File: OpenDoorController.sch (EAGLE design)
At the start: 1 part, among them U1 ATMEGA2560AU

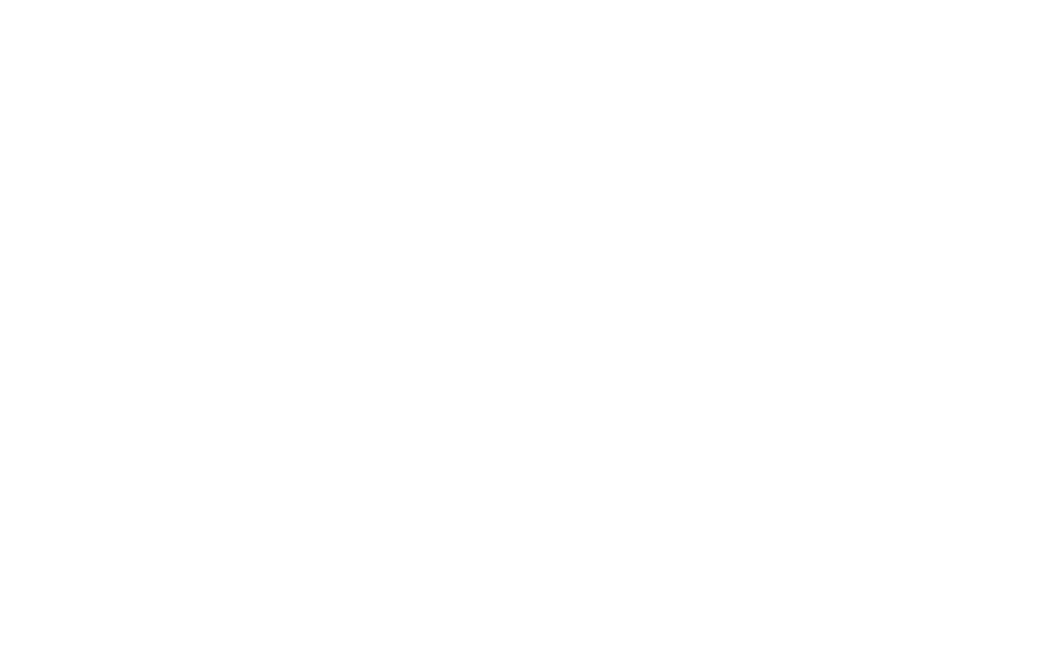
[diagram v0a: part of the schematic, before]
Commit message: Started implementing SMPS and created custom library for esoteric parts
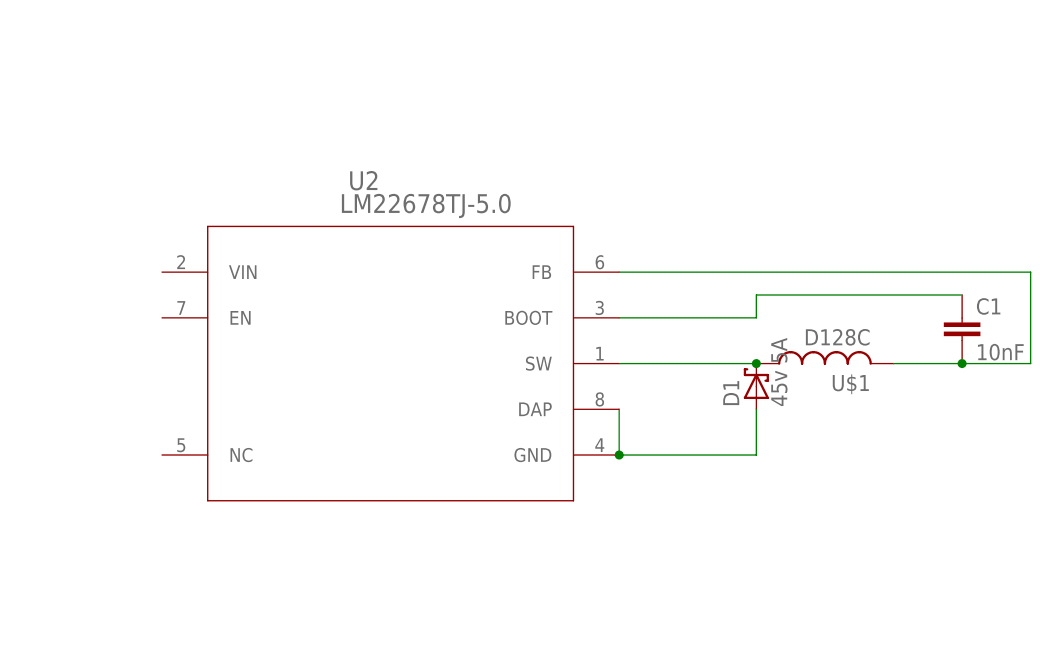
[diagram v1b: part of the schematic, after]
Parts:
- added C1: 10nF, rcl:C-EUC1206
- added D1: 45v 5A, diode:SCHOTTKY-DIODESMC
- added U$1: D128C, CustomSymbols:D128C
- added U2: LM22678TJ-5.0, CustomSymbols:LM22678TJ-5.0
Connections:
- new net N$1: D1.C, U$1.1, U2.SW
- new net N$2: C1.1, U2.BOOT
- new net N$3: C1.2, U$1.2, U2.FB
- new net N$4: D1.A, U2.DAP, U2.GND
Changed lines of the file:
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@@
 <?xml version="1.0" encoding="utf-8"?>
 <!DOCTYPE eagle SYSTEM "eagle.dtd">
-<eagle version="6.1">
+<eagle version="6.2">
 <drawing>
 <settings>
@@
 <parts>
 <part name="U1" library="SparkFun" deviceset="ATMEGA2560" device="AU"/>
+<part name="U2" library="CustomSymbols" deviceset="LM22678TJ-5.0" device=""/>
+<part name="U$1" library="CustomSymbols" deviceset="D128C" device="">
+<attribute name="STOCKNUM" value="724-4890"/>
+<attribute name="SUPPLIER" value="RS Components"/>
+</part>
+<part name="C1" library="rcl" deviceset="C-EU" device="C1206" value="10nF"/>
+<part name="D1" library="diode" deviceset="SCHOTTKY-DIODE" device="SMC" value="45v 5A"/>
 </parts>
 <sheets>
@@
 <instances>
 <instance part="U1" gate="1" x="60.96" y="96.52"/>
+<instance part="U2" gate="A" x="144.78" y="68.58"/>
+<instance part="U$1" gate="G$1" x="218.44" y="58.42" rot="R90">
+<attribute name="STOCKNUM" x="218.44" y="58.42" size="1.778" layer="96" rot="R90" display="off"/>
+<attribute name="SUPPLIER" x="218.44" y="58.42" size="1.778" layer="96" rot="R90" display="off"/>
+</instance>
+<instance part="C1" gate="G$1" x="233.68" y="63.5"/>
+<instance part="D1" gate="G$1" x="210.82" y="55.88" rot="R90"/>
 </instances>
 <busses>
 </busses>
 <nets>
+<net name="N$1" class="0">
+<segment>
+<pinref part="U2" gate="A" pin="SW"/>
+<pinref part="U$1" gate="G$1" pin="1"/>
+<wire x1="195.58" y1="58.42" x2="210.82" y2="58.42" width="0.1524" layer="91"/>
+<pinref part="D1" gate="G$1" pin="C"/>
+<junction x="210.82" y="58.42"/>
+</segment>
+</net>
+<net name="N$2" class="0">
+<segment>
+<pinref part="U2" gate="A" pin="BOOT"/>
+<wire x1="195.58" y1="63.5" x2="210.82" y2="63.5" width="0.1524" layer="91"/>
+<wire x1="210.82" y1="63.5" x2="210.82" y2="66.04" width="0.1524" layer="91"/>
+<pinref part="C1" gate="G$1" pin="1"/>
+<wire x1="210.82" y1="66.04" x2="233.68" y2="66.04" width="0.1524" layer="91"/>
+</segment>
+</net>
+<net name="N$3" class="0">
+<segment>
+<pinref part="U$1" gate="G$1" pin="2"/>
+<pinref part="C1" gate="G$1" pin="2"/>
+<wire x1="226.06" y1="58.42" x2="233.68" y2="58.42" width="0.1524" layer="91"/>
+<pinref part="U2" gate="A" pin="FB"/>
+<wire x1="195.58" y1="68.58" x2="241.3" y2="68.58" width="0.1524" layer="91"/>
+<wire x1="241.3" y1="68.58" x2="241.3" y2="58.42" width="0.1524" layer="91"/>
+<wire x1="241.3" y1="58.42" x2="233.68" y2="58.42" width="0.1524" layer="91"/>
+<junction x="233.68" y="58.42"/>
+</segment>
+</net>
+<net name="N$4" class="0">
+<segment>
+<pinref part="U2" gate="A" pin="GND"/>
+<pinref part="D1" gate="G$1" pin="A"/>
+<wire x1="195.58" y1="48.26" x2="210.82" y2="48.26" width="0.1524" layer="91"/>
+<wire x1="210.82" y1="48.26" x2="210.82" y2="53.34" width="0.1524" layer="91"/>
+<pinref part="U2" gate="A" pin="DAP"/>
+<wire x1="195.58" y1="53.34" x2="195.58" y2="48.26" width="0.1524" layer="91"/>
+<junction x="195.58" y="48.26"/>
+</segment>
+</net>
 </nets>
 </sheet>
 </sheets>
+<errors>
+</errors>
 </schematic>
 </drawing>

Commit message: Cleanup, AVR support stuff and WIZnet stuff started
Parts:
- added C2: 180uF, rcl:CPOL-EU153CLV-0810
- added C3, C4, C5, C6: 100nF, rcl:C-EUC0805
- added COL, FDX, LINK, RX, SPD, TX: (no value), led:LEDCHIPLED_0805
- added IC1: DS3231/SO, adafruit:DS3231/SO
- added R1: 1M, rcl:R-US_M1206
- added RESET: (no value), SparkFun:TAC_SWITCHSMD
- added U$2: (no value), adafruit:CR2032SMT
- added U$3: AVR_SPI_PROG2SMD, SparkFun:AVR_SPI_PROG2SMD
- added U3: (no value), SparkFun:W5100
- added Y1: RESONATORSMD, SparkFun:RESONATORSMD
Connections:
- new net (AREF): C6.1, U1.AREF
- new net (AVR_RESET): RESET.3, RESET.4, U$3.5, U1.RESET
- new net (MISO): U$3.9, U1.(MISO/PCINT3)PB3, U3.MISO
- new net (MOSI): U$3.1, U1.(MOSI/PCINT2)PB2, U3.MOSI
- new net (SCL): IC1.SCL, U1.(SCL/INT0)PD0
- new net (SCLK): U$3.7, U1.(SCK/PCINT1)PB1, U3.SCLK
- new net (SDA): IC1.SDA, U1.(SDA/INT1)PD1
- new net +3V3: U3.3V3A, U3.3V3D@0, U3.3V3D@1, U3.3V3D@2
- new net +5V: C1.2, C2.+, C3.1, C4.1, C5.1, U$1.2, U$3.2, U1.AVCC, U1.VCC, U1.VCC3, U2.FB
- new net GND: C2.-, C3.2, C4.2, C5.2, C6.2, COL.C, D1.A, FDX.C, IC1.GND, IC1.NC, IC1.NC1, IC1.NC2, IC1.NC3, IC1.NC4, IC1.NC5, IC1.NC6, IC1.NC7, LINK.C, RESET.1, RX.C, SPD.C, TX.C, U$2.+, U$2.+1, U$3.10, U$3.4, U$3.6, U$3.8, U1.AGND, U1.GND, U1.GND3, U2.DAP, U2.GND, U3.ADDR0, U3.ADDR1, U3.ADDR10, U3.ADDR11, U3.ADDR12, U3.ADDR13, U3.ADDR14, U3.ADDR2, U3.ADDR3, U3.ADDR4, U3.ADDR5, U3.ADDR6, U3.ADDR7, U3.ADDR8, U3.ADDR9, U3.DATA0, U3.DATA1, U3.DATA2, U3.DATA3, U3.DATA4, U3.DATA5, U3.DATA6, U3.DATA7, U3.GNDA@0, U3.GNDA@1, U3.GNDA@2, U3.GNDD@0, U3.GNDD@1, U3.GNDD@2, U3.GNDD@3, U3.GNDD@4, U3.GNDD@5, U3.OPMODE0, U3.OPMODE1, U3.OPMODE2, U3.TEST0, U3.TEST1, U3.TEST2, U3.TEST3, Y1.2
- new net N$10: IC1.VBAT, U$2.-
- new net N$16: LINK.A, U3.LINKLED
- new net N$18: SPD.A, U3.SPDLED
- new net N$19: FDX.A, U3.FDXLED
- new net N$20: COL.A, U3.COLLED
- new net N$21: RX.A, U3.RXLED
- new net N$22: TX.A, U3.TXLED
- new net N$5: U3.1V8A@0, U3.1V8A@1, U3.1V8D@0, U3.1V8D@1, U3.1V8D@2, U3.1V8D@3, U3.1V8OUT
- new net VCC: U2.VIN
- net N$3: now also R1.1, U1.XTAL1, Y1.3; no longer C1.2, U$1.2, U2.FB
- net N$4: now also R1.2, U1.XTAL2, Y1.1; no longer D1.A, U2.DAP, U2.GND
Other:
- moved on the sheet: C1, D1, U$1, U2

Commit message: More stuff implemented, I should sleep.
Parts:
- removed FDX, LINK: (no value), led:LEDCHIPLED_0805
- added C10, C11, C12: 0.1uF, rcl:C-EUC0805
- added C13: 470pF, rcl:C-EUC0805
- added C14: 2.2uF, rcl:C-EUC0805
- added C7, C8: 22pF, rcl:C-EUC0805
- added C9: 100nF, rcl:C-EUC0805
- added JP1: FTDI_BASICPTH, SparkFun:FTDI_BASICPTH
- added Q1: 25MHz, crystal:CRYSTALSM49
- added Q2: IRLML5203, transistor-power:IRLML5203
- added R10, R11, R12, R7, R8, R9: 470R, rcl:R-US_M0805
- added R13: 100R, rcl:R-US_M0805
- added R14: 10K, pot:TRIM_US-SM-42/43W
- added R15: 12K, rcl:R-US_M0805
- added R16: 300R, rcl:R-US_M0805
- added R17: 1k, rcl:R-US_M0805
- added R2: 1M, rcl:R-US_M1206
- added R3, R4, R5, R6: 49.9, rcl:R-US_M0805
- added STRIKE: (no value), con-wago-500:W237-102
- added U4: MAGJACK-POE, SparkFun:MAGJACK-POE
- added U5: MIC5205-3.3BM, SparkFun:V_REG_LDOSMD
- added X1: HD44780LCD-1602, adafruit:HD44780LCD-1602
- U$3: value AVR_SPI_PROG2SMD -> AVR_SPI_PROG2PTH2; device SparkFun:AVR_SPI_PROG2SMD -> SparkFun:AVR_SPI_PROG2PTH2
- Y1: value RESONATORSMD -> CSTCE16
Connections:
- net (AREF) renamed N$6
- new net (RX0): JP1.2, U1.(RXD0/PCIN8)PE0
- new net (RX1): U1.(SS/PCINT0)PB0
- new net (TX0): JP1.3, U1.(TXD0)PE1
- new net (TX1): U1.PH6(OC2B)
- new net FDXLED: U3.FDXLED, U4.YLED-
- new net LINKLED: U3.LINKLED, U4.GLED-
- new net N$11: C8.1, Q1.1, R2.1, U3.XTLP
- new net N$12: C12.2, R5.2, R6.2
- new net N$13: R8.1, U4.YLED+
- new net N$14: C11.2, R3.2, R4.2
- new net N$15: R7.1, U4.GLED+
- new net N$17: R10.2, RX.A
- new net N$23: TX.C, U3.TXLED
- new net N$24: R14.S, X1.VO
- new net N$25: R13.2, X1.A
- new net N$26: R15.1, U3.RSET_BG
- new net N$27: R15.2, R16.1
- new net N$28: R17.1, U3.*CS, U3.*RD, U3.*WR
- new net N$29: C13.1, U5.BP
- new net N$7: Q2.D, STRIKE-2.KL
- new net N$8: C7.1, Q1.2, R2.2, U3.XTLN
- new net N$9: C9.1, JP1.1
- new net RXIN: R3.1, U3.RXIN
- new net RXIP: R4.1, U3.RXIP
- new net TXON: R5.1, U3.TXON, U4.TD-
- new net TXOP: R6.1, U3.TXOP, U4.TD+
- new net WIZ_PWR_EN: U5.EN
- new net WIZ_RESET: U3.*RESET
- new net [A13]: U1.PK5(ADC13/PCINT21)
- new net [A14]: U1.PK6(ADC14/PCINT22)
- new net [A15]: U1.PK7(ADC15/PCINT23)
- new net [D30]: U1.(A15)PC7, X1.RS
- new net [D31]: U1.(A14)PC6, X1.E
- new net [D32]: U1.(A13)PC5, X1.DB4
- new net [D33]: U1.(A12)PC4, X1.DB5
- new net [D34]: U1.(A11)PC3, X1.DB6
- new net [D35]: U1.(A10)PC2, X1.DB7
- new net [D36]: U1.(A9)PC1
- new net [D38]: U1.(A8)PC0
- new net [D62]: U1.PK0(ADC8/PCINT16)
- new net [D63]: U1.PK1(ADC9/PCINT17)
- new net [D64]: U1.PK2(ADC10/PCINT18)
- new net [D65]: U1.PK3(ADC11/PCINT19)
- new net [D66]: U1.PK4(ADC12/PCINT20), U3.*INT
- net (AVR_RESET): now also C9.2
- net +3V3: now also C10.1, C14.1, R10.1, R11.1, R12.1, R17.2, R7.2, R8.2, R9.1, U4.TCT, U5.OUT
- net +5V: now also IC1.VCC, JP1.4, R14.A, U1.VCC1, U1.VCC2, U5.IN, X1.VDD
- net GND: now also C10.2, C11.1, C12.1, C13.2, C14.2, C7.2, C8.2, JP1.6, R14.E, R16.2, RESET.2, STRIKE-1.KL, U1.GND1, U1.GND2, U4.SHIELD@0, U4.SHIELD@1, U5.GND, X1.K, X1.VSS; no longer COL.C, FDX.C, LINK.C, RX.C, SPD.C, TX.C
- net N$16: now also R9.2, TX.A; no longer LINK.A, U3.LINKLED
- net N$18: now also COL.A, R11.2; no longer SPD.A, U3.SPDLED
- net N$19: now also R12.2, SPD.A; no longer FDX.A, U3.FDXLED
- net N$20: now also SPD.C, U3.SPDLED; no longer COL.A, U3.COLLED
- net N$21: now also COL.C, U3.COLLED; no longer RX.A, U3.RXLED
- net N$22: now also RX.C, U3.RXLED; no longer TX.A, U3.TXLED
- net VCC: now also Q2.S
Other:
- moved on the sheet: C3, C4, C5, C6, COL, IC1, R1, RESET, RX, SPD, TX, U$2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
